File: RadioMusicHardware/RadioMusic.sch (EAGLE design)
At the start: 62 parts, among them IC2 7805L, IC3 TL072P, IC4 TL072P

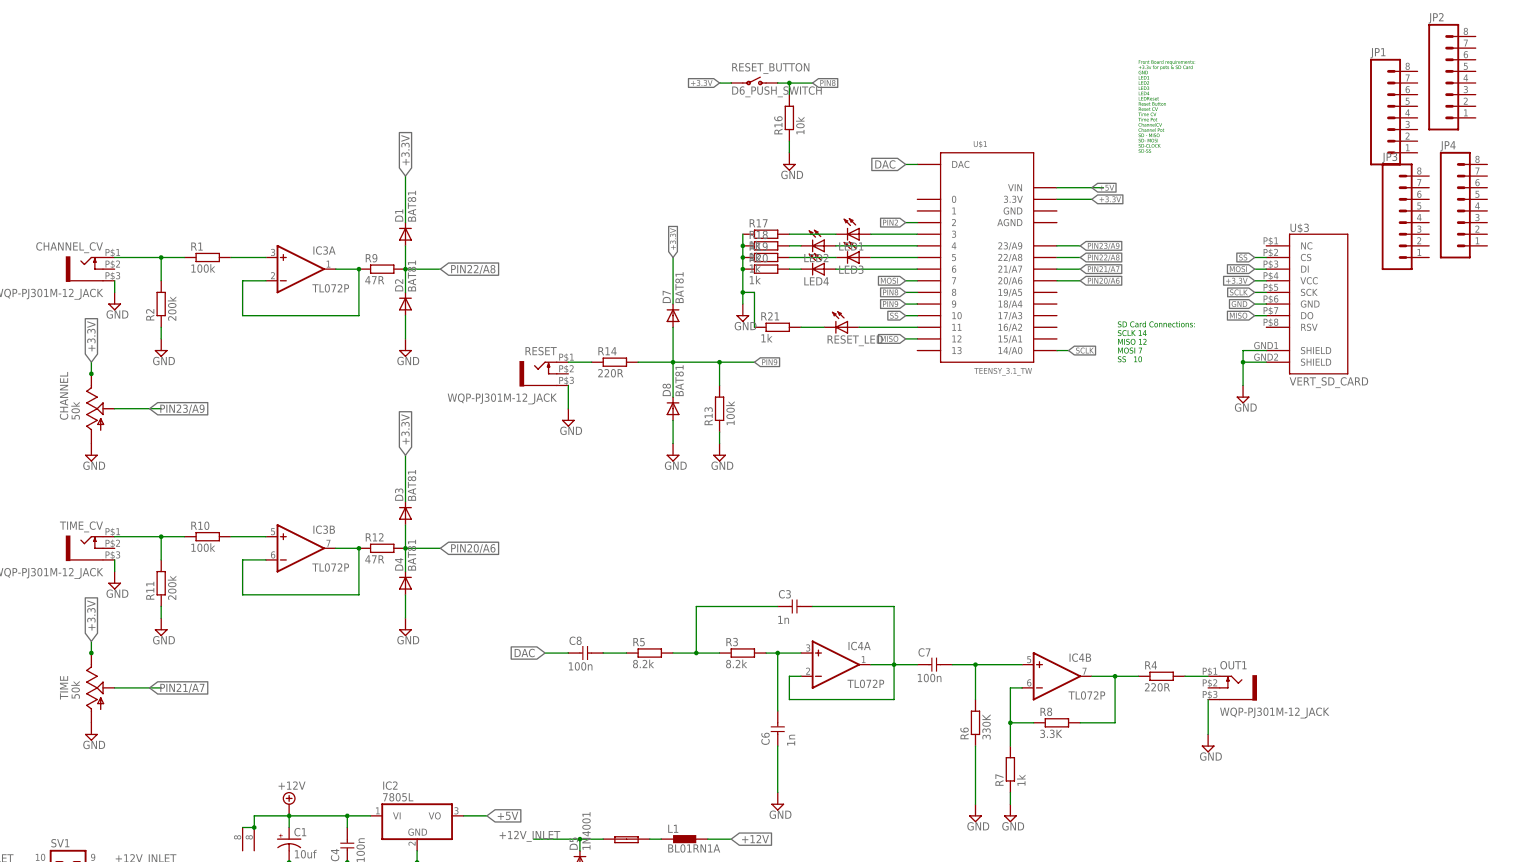
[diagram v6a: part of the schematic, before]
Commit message: split signals across back and front
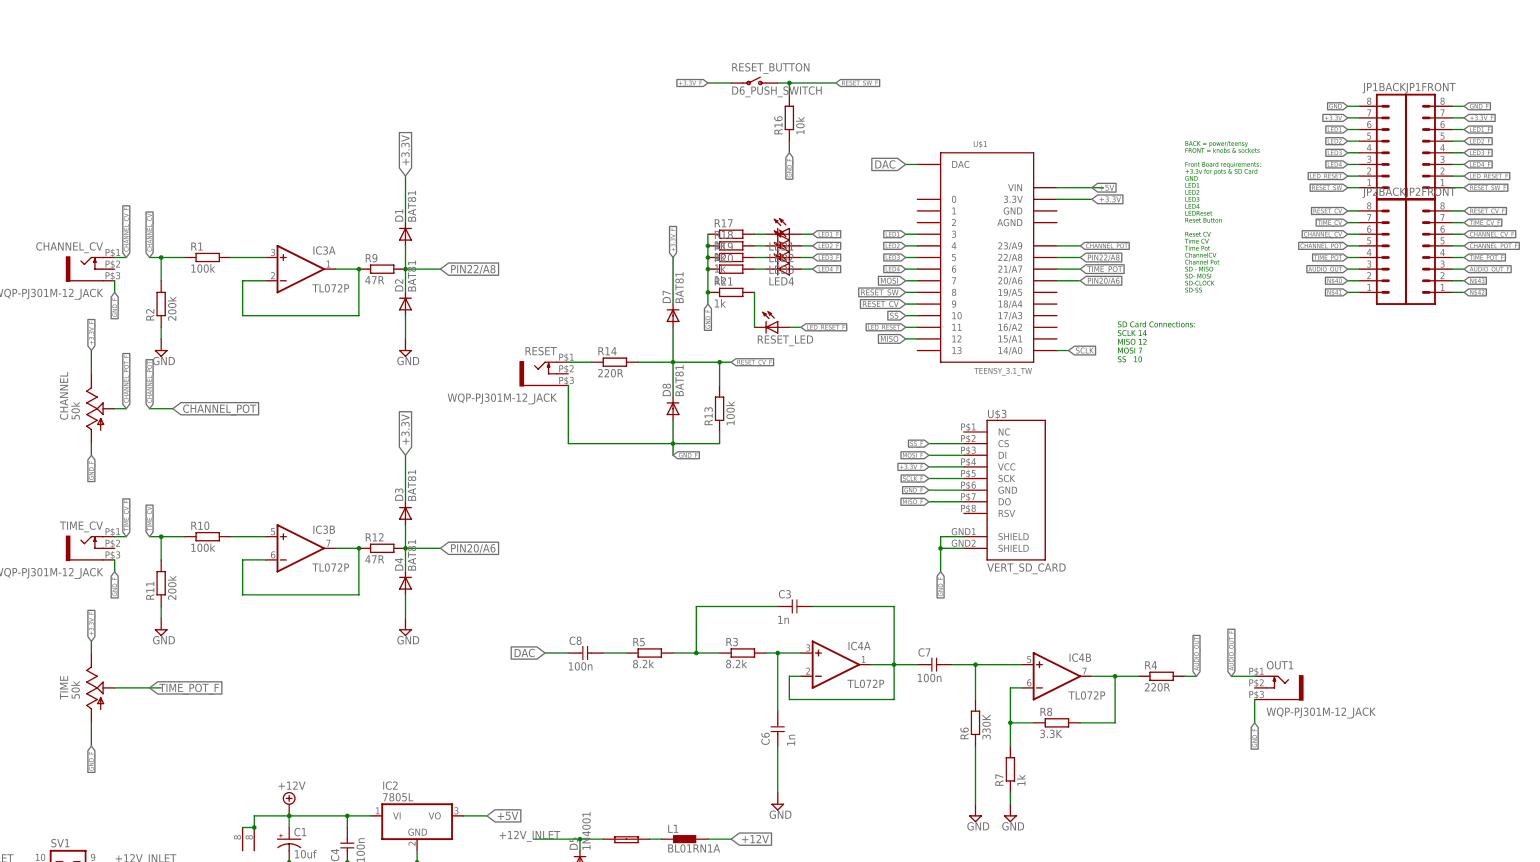
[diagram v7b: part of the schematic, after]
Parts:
- removed JP1, JP2, JP3, JP4: (no value), SparkFun-Connectors:M08LOCK
- added JP1BACK, JP1FRONT, JP2BACK, JP2FRONT: (no value), SparkFun-Connectors:M08LOCK
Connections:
- removed net N$1: CHANNEL_CV.2, R1.1, R2.2
- removed net N$11: R10.1, R11.2, TIME_CV.2
- removed net N$13: LED1.A, U$1.3
- removed net N$15: LED2.A, U$1.4
- removed net N$16: LED3.A, U$1.5
- removed net N$17: LED4.A, U$1.6
- removed net N$24: RESET_LED.A, U$1.11
- removed net N$9: OUT1.2, R4.2
- removed net PIN2: U$1.2
- removed net PIN21/A7: TIME.S, U$1.21/A7
- removed net PIN23/A9: CHANNEL.S, U$1.23/A9
- removed net PIN8: R16.2, RESET_BUTTON.O, U$1.8
- removed net PIN9: D7.A, D8.C, R13.2, R14.2, U$1.9
- new net +3.3V_F: CHANNEL.E, D7.C, JP1FRONT.7, RESET_BUTTON.P, TIME.E, U$3.VCC
- new net AUDIO_OUT: JP2BACK.3, R4.2
- new net AUDIO_OUT_F: JP2FRONT.3, OUT1.2
- new net CHANNEL_CV: JP2BACK.6, R1.1, R2.2
- new net CHANNEL_CV_F: CHANNEL_CV.2, JP2FRONT.6
- new net CHANNEL_POT: JP2BACK.5, U$1.23/A9
- new net CHANNEL_POT_F: CHANNEL.S, JP2FRONT.5
- new net GND_F: CHANNEL.A, CHANNEL_CV.1, D8.A, JP1FRONT.8, OUT1.1, R13.1, R16.1, R17.1, R18.1, R19.1, R20.1, R21.1, RESET.1, TIME.A, TIME_CV.1, U$3.GND, U$3.SHIELD@1, U$3.SHIELD@2
- new net LED1: JP1BACK.6, U$1.3
- new net LED1_F: JP1FRONT.6, LED1.A
- new net LED2: JP1BACK.5, U$1.4
- new net LED2_F: JP1FRONT.5, LED2.A
- new net LED3: JP1BACK.4, U$1.5
- new net LED3_F: JP1FRONT.4, LED3.A
- new net LED4: JP1BACK.3, U$1.6
- new net LED4_F: JP1FRONT.3, LED4.A
- new net LED_RESET: JP1BACK.2, U$1.11
- new net LED_RESET_F: JP1FRONT.2, RESET_LED.A
- new net MISO_F: U$3.DO
- new net MOSI_F: U$3.DI
- new net N$40: JP2BACK.2
- new net N$41: JP2BACK.1
- new net N$42: JP2FRONT.1
- new net N$43: JP2FRONT.2
- new net RESET_CV: JP2BACK.8, U$1.9
- new net RESET_CV_F: D7.A, D8.C, JP2FRONT.8, R13.2, R14.2
- new net RESET_SW: JP1BACK.1, U$1.8
- new net RESET_SW_F: JP1FRONT.1, R16.2, RESET_BUTTON.O
- new net SCLK_F: U$3.SCK
- new net SS_F: U$3.CS
- new net TIME_CV: JP2BACK.7, R10.1, R11.2
- new net TIME_CV_F: JP2FRONT.7, TIME_CV.2
- new net TIME_POT: JP2BACK.4, U$1.21/A7
- new net TIME_POT_F: JP2FRONT.4, TIME.S
- net +3.3V: now also JP1BACK.7; no longer CHANNEL.E, D7.C, RESET_BUTTON.P, TIME.E, U$3.VCC
- net GND: now also JP1BACK.8; no longer CHANNEL.A, CHANNEL_CV.1, D8.A, OUT1.1, R13.1, R16.1, R17.1, R18.1, R19.1, R20.1, R21.1, RESET.1, TIME.A, TIME_CV.1, U$3.GND, U$3.SHIELD@1, U$3.SHIELD@2
- net MISO: no longer U$3.DO
- net MOSI: no longer U$3.DI
- net SCLK: no longer U$3.SCK
- net SS: no longer U$3.CS
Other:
- note added: "BACK = power/teensy FRONT = knobs & sockets Front Board requirements: +3.3v for pots & SD Card GND LED1 LED2 LED3 LED4 LEDReset Reset Button Reset CV Time CV Time Pot ChannelCV Channel Pot SD - MISO SD- MOSI SD-CLOCK SD-SS"
- note removed: "Front Board requirements: +3.3v for pots & SD Card GND LED1 LED2 LED3 LED4 LEDReset Reset Button Reset CV Time CV Time Pot ChannelCV Channel Pot SD - MISO SD- MOSI SD-CLOCK SD-SS"
- moved on the sheet: LED1, LED2, LED3, LED4, OUT1, R17, R18, R19, R20, R21, RESET_LED, U$3

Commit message: Simple Crossfading
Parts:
- JP2BACK, JP2FRONT: value (none) -> M10LOCK; device SparkFun-Connectors:M08LOCK -> SparkFun-Connectors:M10LOCK
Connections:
- removed net N$40: JP2BACK.2
- removed net N$41: JP2BACK.1
- removed net N$42: JP2FRONT.1
- removed net N$43: JP2FRONT.2
- new net DGND: C4.2, C5.2, D2.A, D4.A, IC2.GND, U$1.GND
- new net N$1: IC3B.-IN, IC3B.OUT, R12.1
- net +12V: now also L1.1; no longer L1.2
- net +3.3V: now also JP2BACK.1; no longer JP1BACK.7
- net +3.3V_F: now also JP2FRONT.1; no longer JP1FRONT.7
- net -12V: now also C5.1, L2.1; no longer C5.2, L2.2
- net AUDIO_OUT: now also JP2BACK.5, R4.1; no longer JP2BACK.3, R4.2
- net AUDIO_OUT_F: now also JP2FRONT.5; no longer JP2FRONT.3
- net CHANNEL_CV: now also JP2BACK.8, R2.1; no longer JP2BACK.6, R2.2
- net CHANNEL_CV_F: now also JP2FRONT.8; no longer JP2FRONT.6
- net CHANNEL_POT: now also JP2BACK.7; no longer JP2BACK.5
- net CHANNEL_POT_F: now also JP2FRONT.7; no longer JP2FRONT.5
- net DAC: now also C8.1; no longer C8.2
- net GND: now also R11.2, R2.2, U$1.AGND; no longer C4.2, C5.1, D2.A, D4.A, IC2.GND, R11.1, R2.1
- net MISO: now also JP2BACK.4
- net MISO_F: now also JP2FRONT.4
- net MOSI: now also JP2BACK.3
- net MOSI_F: now also JP2FRONT.3
- net N$10: now also C8.2; no longer C8.1
- net N$2: now also IC4B.+IN, R3.1; no longer IC4A.+IN, R3.2
- net N$22: now also L1.2; no longer L1.1
- net N$23: now also L2.2; no longer L2.1
- net N$4: now also C3.1, R3.2; no longer C3.2, R3.1
- net N$5: now also C3.2, IC4B.-IN, IC4B.OUT; no longer C3.1, IC4A.-IN, IC4A.OUT
- net N$6: now also IC4A.+IN; no longer IC4B.+IN
- net N$7: now also IC4A.-IN, R8.2; no longer IC4B.-IN, R8.1
- net N$8: now also IC4A.OUT, R4.2, R8.1; no longer IC4B.OUT, R4.1, R8.2
- net PIN22/A8: no longer IC3B.-IN, IC3B.OUT, R12.1
- net RESET_CV: now also JP2BACK.10; no longer JP2BACK.8
- net RESET_CV_F: now also JP2FRONT.10; no longer JP2FRONT.8
- net SCLK: now also JP2BACK.2
- net SCLK_F: now also JP2FRONT.2
- net SS: now also JP1BACK.7
- net SS_F: now also JP1FRONT.7
- net TIME_CV: now also JP2BACK.9, R11.1; no longer JP2BACK.7, R11.2
- net TIME_CV_F: now also JP2FRONT.9; no longer JP2FRONT.7
- net TIME_POT: now also JP2BACK.6; no longer JP2BACK.4
- net TIME_POT_F: now also JP2FRONT.6; no longer JP2FRONT.4
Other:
- note added: "TEST: Should I take AGND to the front panel?"
- moved on the sheet: C4, IC4A, IC4B, L1, L2, R3
